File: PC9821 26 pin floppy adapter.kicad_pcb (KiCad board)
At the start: 2 copper layers, 52.7 x 28.6 mm, 3 parts

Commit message: Final version that I just sent off to Osh
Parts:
- added G***: LOGO, Logos:skull-silk, B.Cu at (149.9, 92.7)
- PC98-F1: footprint Connector_IDC:IDC-Header_2x13_P2.54mm_Vertical -> Connector_IDC:IDC-Header_2x13_P2.54mm_Horizontal
- moved POWER1 27.5 mm to (151.8, 69.8), turned to 0 degrees
- moved PC98-F1 24.7 mm to (160.7, 78.7), turned to 0 degrees
- moved GOTEK1 13.5 mm to (139.7, 114.3), turned to 180 degrees
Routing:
- net /WRITE_PROTECT: track 13.9 -> 70.7 mm
- net /TRACK_00: track 13.9 -> 67.9 mm
- net /INDEX_OUT: track 13.9 -> 63.3 mm
- net /SIDE: track 13.9 -> 57.5 mm
- net /WRITE_ENABLE: track 13.9 -> 54.5 mm
- net /READ_DATA: track 13.9 -> 53.4 mm
- net /WRITE_DATA: track 13.9 -> 49.1 mm
- net /DRV_SELECT_0: track 13.9 -> 44.5 mm
- net /STEP_PULSE: track 13.9 -> 39.4 mm, vias 0 -> 2
- net /MOTOR_ON: track 13.9 -> 33.5 mm, vias 0 -> 2
- net /HEAD_LOAD: track 54.9 -> 36.1 mm
- net /DIRECTION: track 14.0 -> 28.1 mm
- net /DRV_SELECT_1: track 17.7 -> 29.8 mm
- net /360_300_DRV_0: track 102.5 -> 114.6 mm, vias 0 -> 4
- net /READY_OUT: track 47.4 -> 36.3 mm, vias 0 -> 1
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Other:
- board size 52.7 x 28.6 mm -> 33.7 x 49.5 mm
- board text added: "25"
- board text added: "34"
- board text added: "nec pc-9821 34-pin floppy adapter v1.0"
- board text added: "www.leadedsolder.com"
- board text removed: "2"
- board text removed: "26"
- board text removed: "33"
- board text removed: "key this end"
- board text removed: "leadedsolder.com"
- board text removed: "pc9821 floppy adapter v1.0"

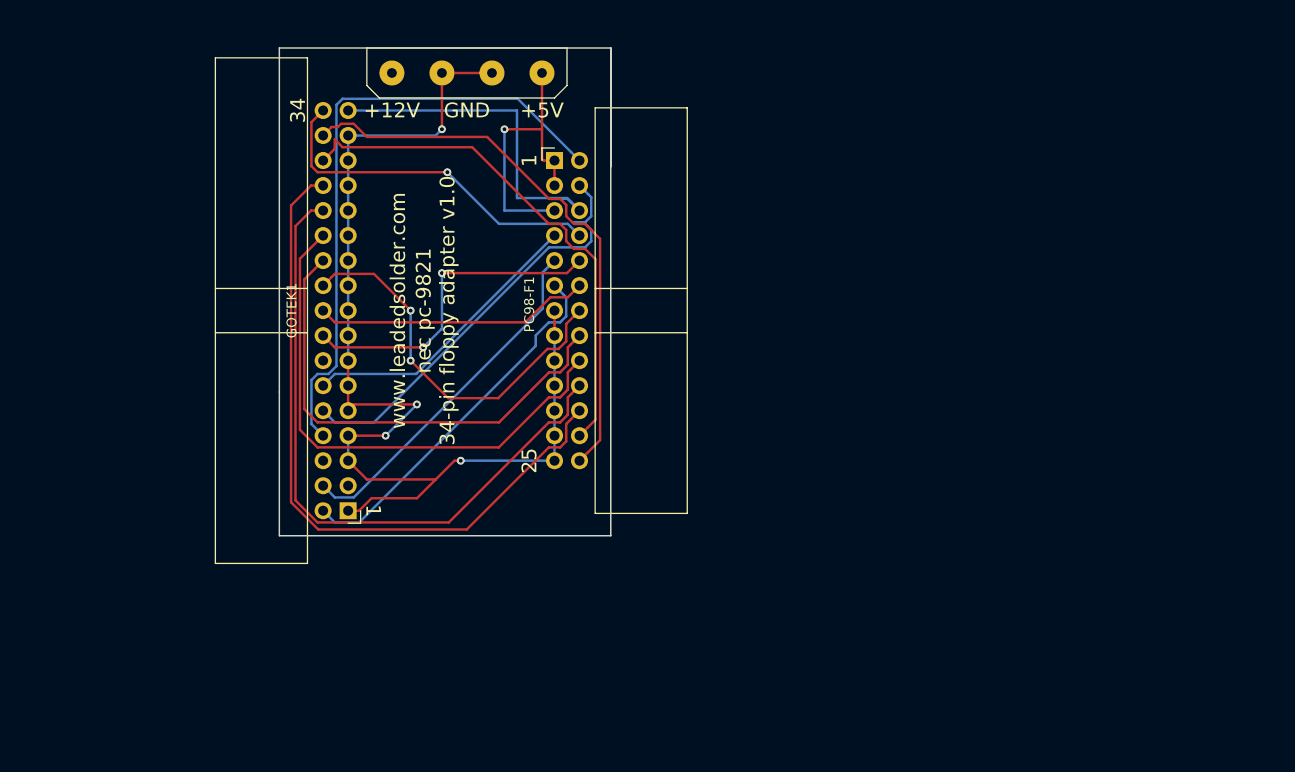
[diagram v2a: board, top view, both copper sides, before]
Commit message: v1.1, a huge ridiculous board that doesn't have a molex power connector on it anymore
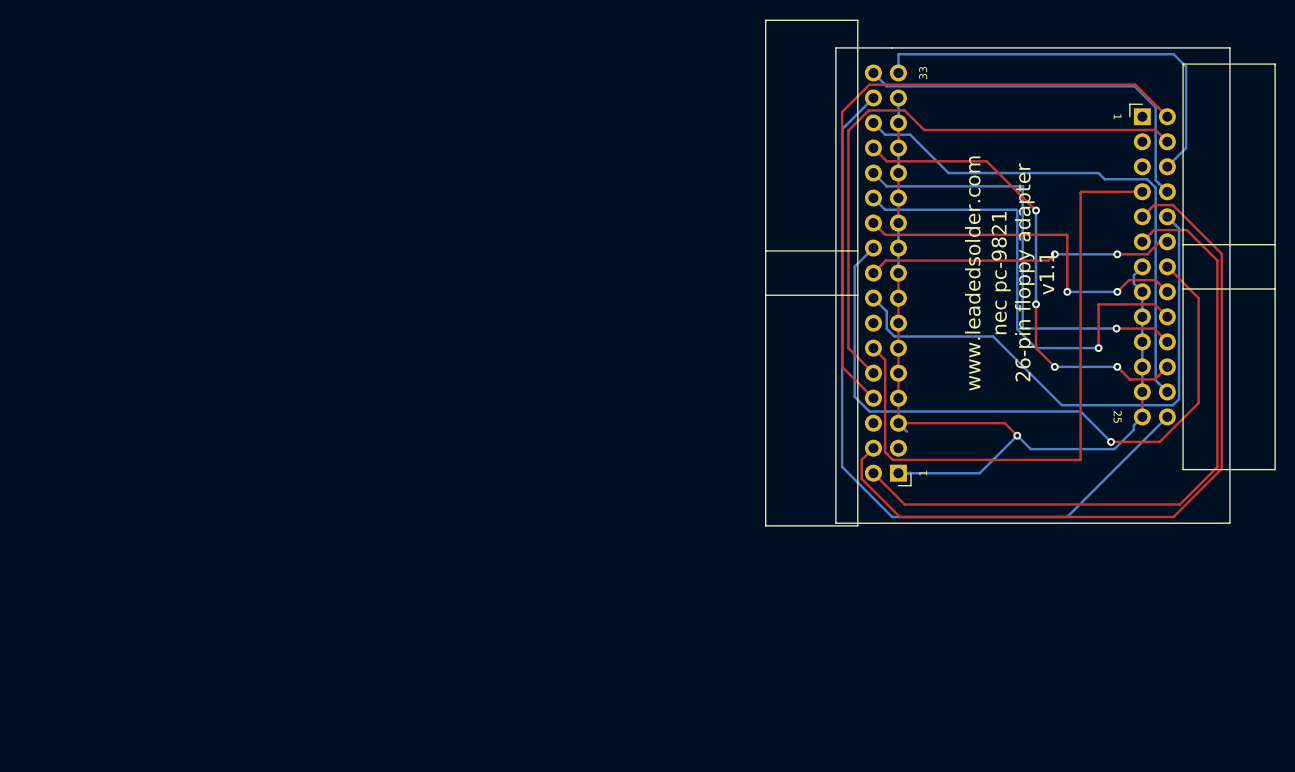
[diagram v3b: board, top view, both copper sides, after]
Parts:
- removed POWER1: 4 pin male molex power, XESS connector lib:xess-MOLEX-8981-04P
- moved PC98-F1 59.9 mm to (220.3, 74.3)
- moved G*** 56.6 mm to (206.4, 90.2)
- moved GOTEK1 56.0 mm to (195.6, 110.5)
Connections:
- PC98-F1 pad 1: /+5V -> /+5V_1
- PC98-F1 pad 3: /+5V -> /+5V_2
- PC98-F1 pad 5: /+5V -> /+5V_3
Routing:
- net /HEAD_LOAD: track 36.1 -> 76.2 mm
- net /DRV_SELECT_1: track 29.8 -> 64.7 mm
- net /DENSITY: track 38.1 -> 68.2 mm
- net /STEP_PULSE: track 39.4 -> 69.5 mm, vias 2 -> 1
- net /+5V: track 29.8 -> 0.00 mm, vias 1 -> 0
- net /WRITE_PROTECT: track 70.7 -> 48.3 mm, vias 0 -> 4
- net /MOTOR_ON: track 33.5 -> 55.8 mm, vias 2 -> 0
- net /TRACK_00: track 67.9 -> 45.6 mm, vias 0 -> 1
- net /360_300_DRV_0: track 114.6 -> 92.5 mm, vias 4 -> 1
- net /SIDE: track 57.5 -> 78.1 mm
- net /DRV_SELECT_0: track 44.5 -> 60.2 mm
- net /WRITE_DATA: track 49.1 -> 37.1 mm, vias 0 -> 2
- net /WRITE_ENABLE: track 54.5 -> 48.2 mm, vias 0 -> 1
- net /DISK_CHANGE: track 36.5 -> 42.6 mm
- net /DIRECTION: track 28.1 -> 31.2 mm, vias 0 -> 2
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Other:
- board size 33.7 x 49.5 mm -> 40 x 48.3 mm
- board text added: "33"
- board text added: "360/300"
- board text added: "nec pc-9821 26-pin floppy adapter v1.1"
- board text removed: "+12V"
- board text removed: "+5V"
- board text removed: "34"
- board text removed: "GND"
- board text removed: "nec pc-9821 34-pin floppy adapter v1.0"

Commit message: Minaturized version, now only 7.95 instead of 15.05
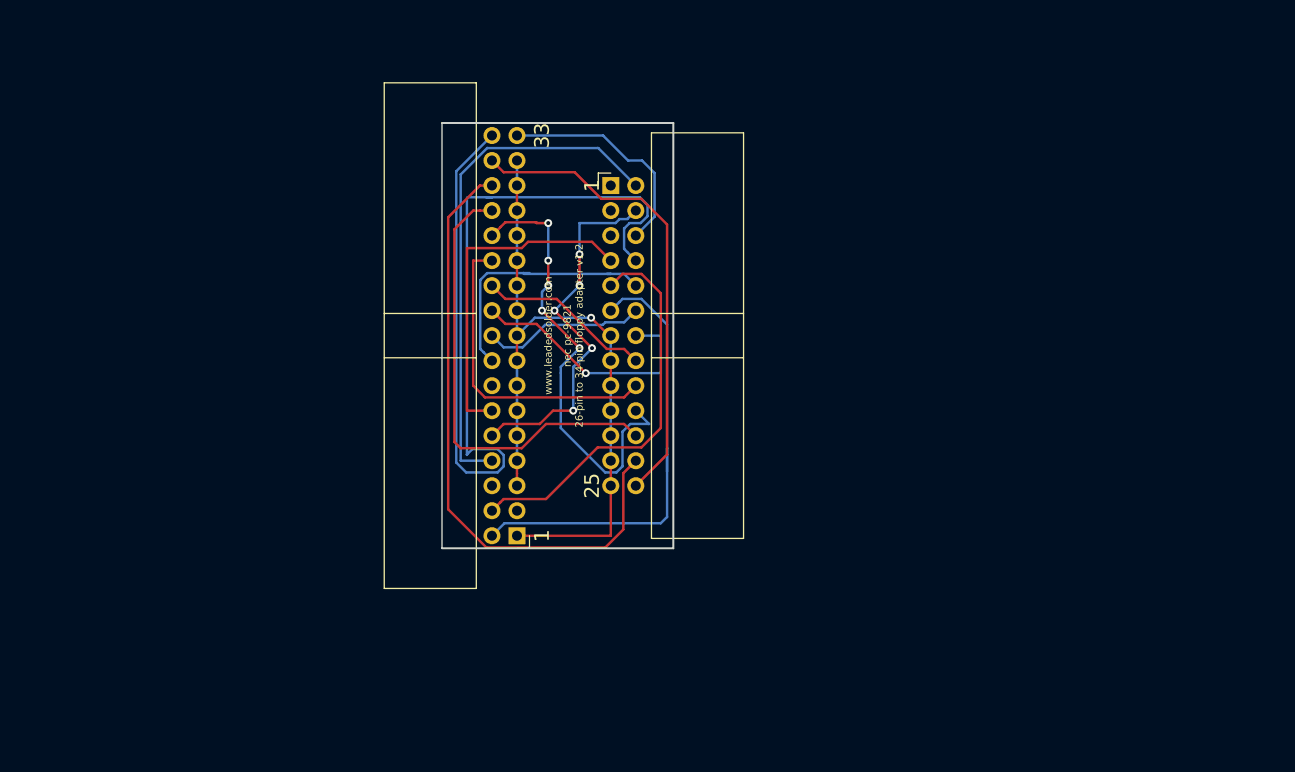
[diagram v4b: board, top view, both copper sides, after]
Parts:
- removed G***: LOGO, Logos:skull-silk
- moved PC98-F1 54.4 mm to (166.4, 81.3)
- moved GOTEK1 39.3 mm to (156.8, 116.8)
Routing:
- net /READY_OUT: track 39.2 -> 98.9 mm
- net /STEP_PULSE: track 69.5 -> 26.1 mm
- net /HEAD_LOAD: track 76.2 -> 40.7 mm
- net /DRV_SELECT_1: track 64.7 -> 34.7 mm
- net /SIDE: track 78.1 -> 48.3 mm
- net /MOTOR_ON: track 55.8 -> 26.3 mm
- net /DRV_SELECT_0: track 60.2 -> 38.0 mm, vias 0 -> 5
- net /DENSITY: track 68.2 -> 47.8 mm
- net /DISK_CHANGE: track 42.6 -> 22.7 mm
- net /WRITE_DATA: track 37.1 -> 17.8 mm, vias 2 -> 0
- net /360_300_DRV_0: track 92.5 -> 73.9 mm
- net /WRITE_ENABLE: track 48.2 -> 32.1 mm, vias 1 -> 0
- net /DIRECTION: track 31.2 -> 16.6 mm, vias 2 -> 0
- net /INDEX_OUT: track 65.9 -> 52.7 mm
- net /READ_DATA: track 52.6 -> 63.8 mm
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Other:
- board size 40 x 48.3 mm -> 23.5 x 43.2 mm
- board text added: "idc 34-pin female"
- board text added: "nec 26-pin male"
- board text added: "nec pc-9821 26-pin to 34-pin floppy adapter v1.2"
- board text removed: "360/300"
- board text removed: "nec pc-9821 26-pin floppy adapter v1.1"

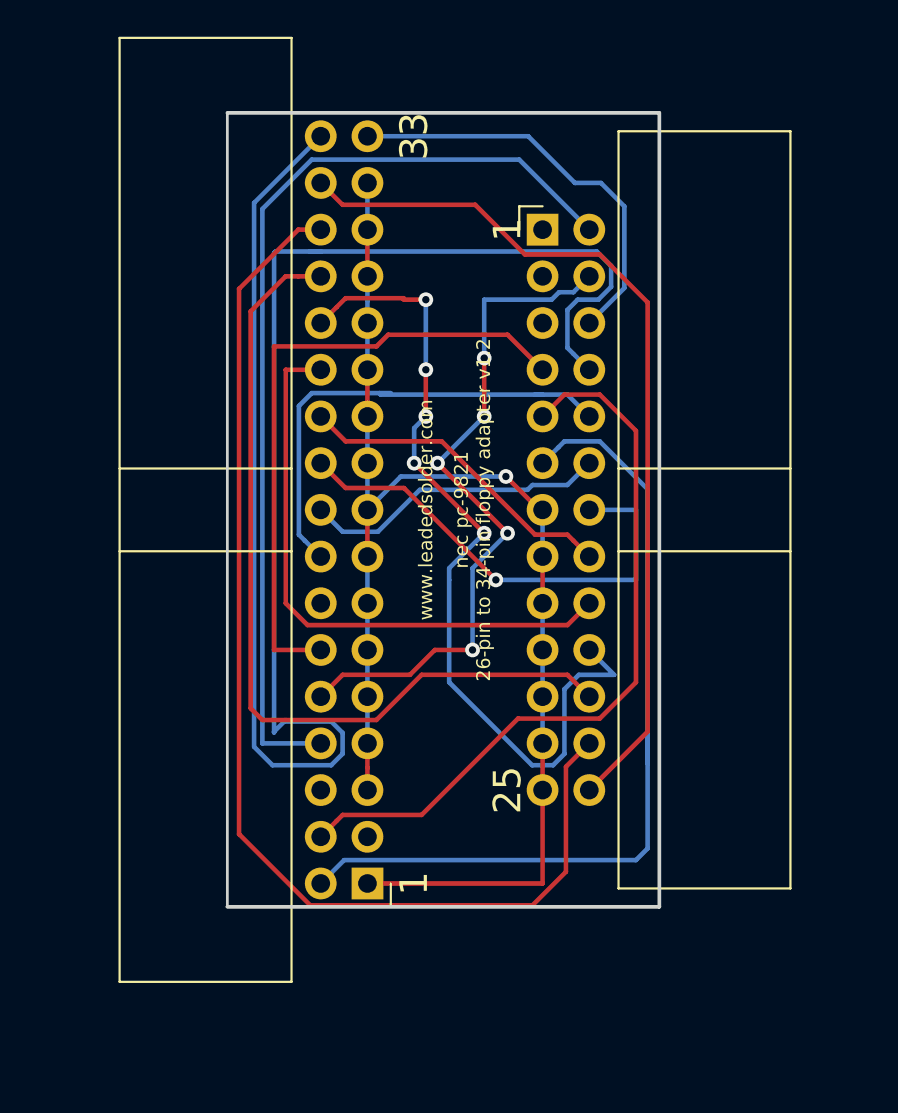
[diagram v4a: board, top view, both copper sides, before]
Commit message: A revision with a Molex 8981 power connector to provide power OUT to the 34-pin floppy drive
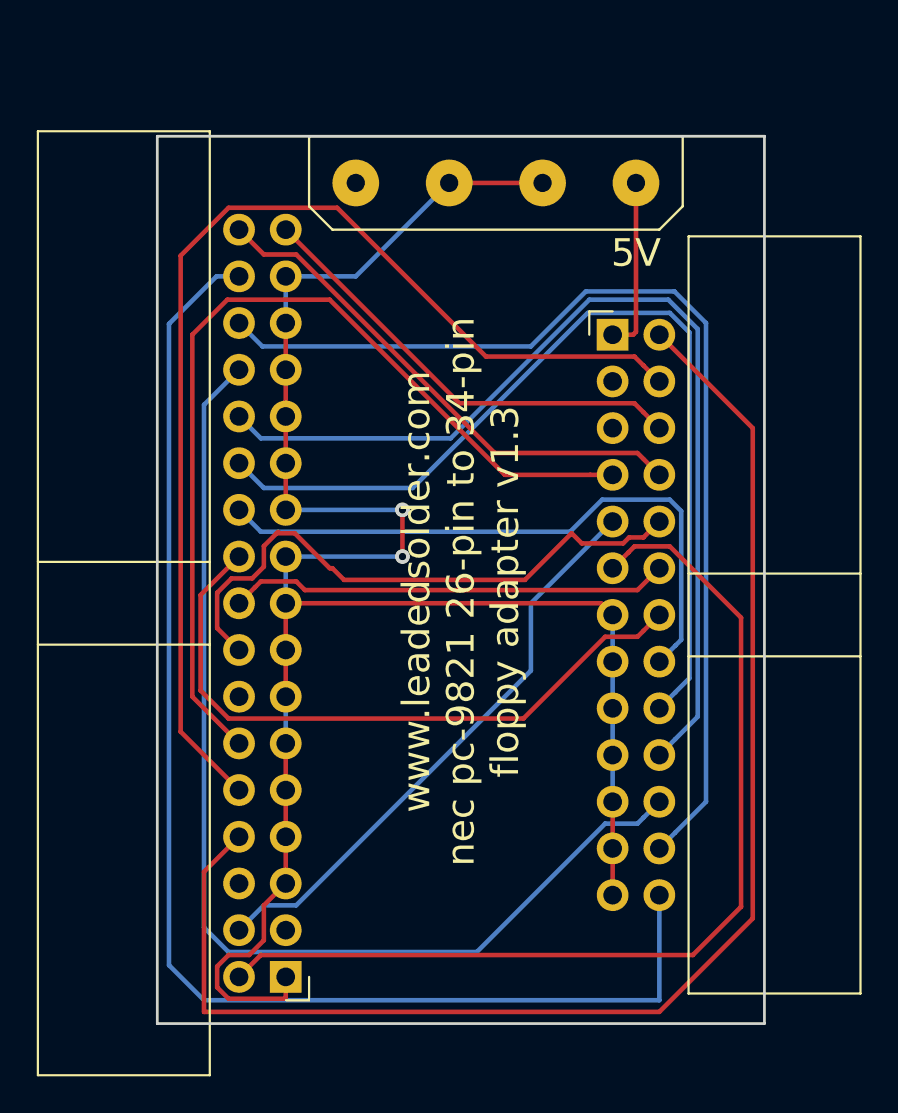
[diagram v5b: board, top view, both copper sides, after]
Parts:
- added PWR1: Molex 8981 Power Out, XESS connector lib:xess-MOLEX-8981-04P, F.Cu at (163.8, 78.7)
- moved PC98-F1 6.87 mm to (170.2, 87.0)
- moved GOTEK1 6.75 mm to (152.4, 121.9)
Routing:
- net /READY_OUT: track 98.9 -> 28.4 mm
- net /360_300_DRV_0: track 73.9 -> 108.1 mm, vias 1 -> 2
- net /SIDE: track 48.3 -> 72.9 mm
- net /INDEX_OUT: track 52.7 -> 76.1 mm
- net /DRV_SELECT_0: track 38.0 -> 61.4 mm, vias 5 -> 0
- net /WRITE_ENABLE: track 32.1 -> 50.6 mm
- net /WRITE_DATA: track 17.8 -> 34.2 mm
- net /DRV_SELECT_1: track 34.7 -> 50.9 mm
- net /WRITE_PROTECT: track 46.4 -> 59.8 mm
- net /STEP_PULSE: track 26.1 -> 36.1 mm, vias 1 -> 0
- net /+5V_1: track 0.00 -> 9.43 mm
- net /HEAD_LOAD: track 40.7 -> 31.7 mm
- net /DIRECTION: track 16.6 -> 24.0 mm
- net /TRACK_00: track 46.7 -> 53.3 mm, vias 5 -> 0
- net /READ_DATA: track 63.8 -> 57.5 mm
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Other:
- board size 23.5 x 43.2 mm -> 33 x 48.3 mm
- board text added: "5V"
- board text added: "POWER OUT"
- board text added: "www.leadedsolder.com nec pc-9821 26-pin to 34-pin floppy adapter v1.3"
- board text removed: "idc 34-pin female"
- board text removed: "nec 26-pin male"
- board text removed: "nec pc-9821 26-pin to 34-pin floppy adapter v1.2"
- board text removed: "www.leadedsolder.com"

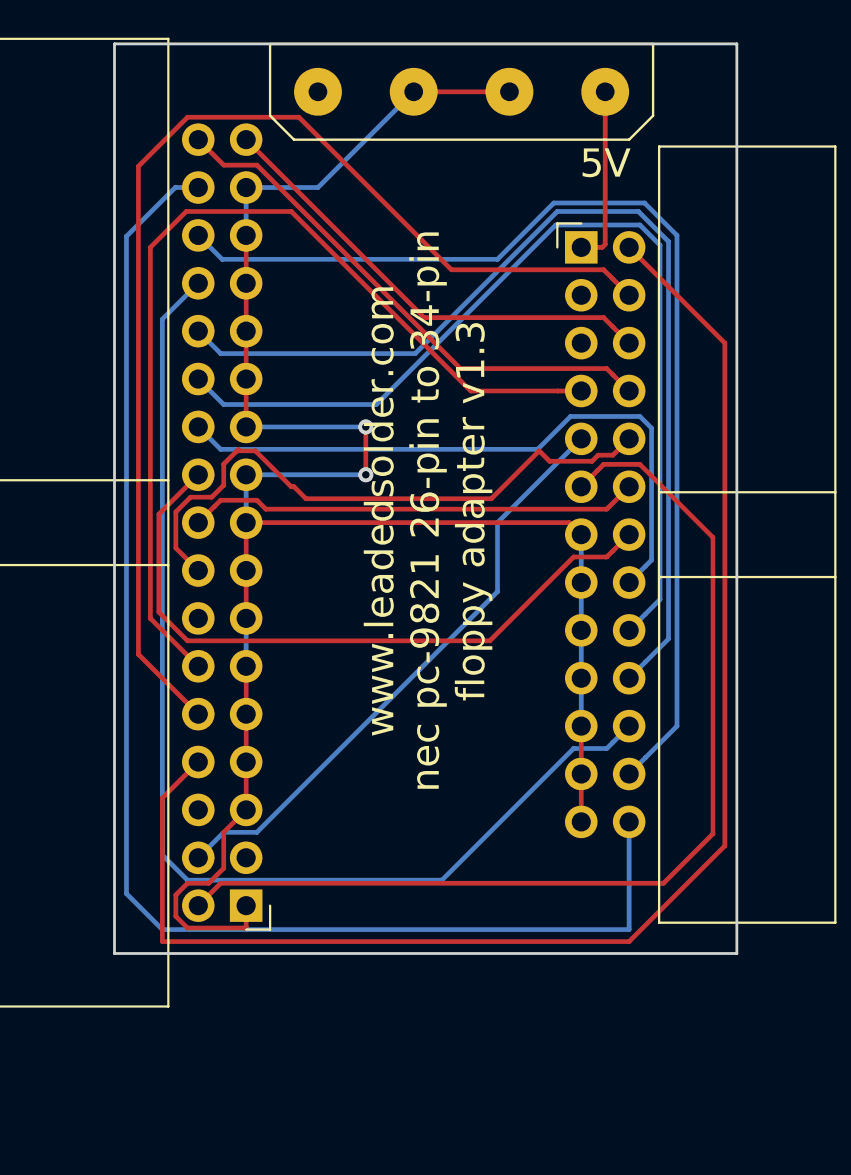
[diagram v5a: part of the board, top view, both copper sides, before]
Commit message: Revision 1.4 - has bigger holes for the Molex connector, and the Molex connector is on the other side
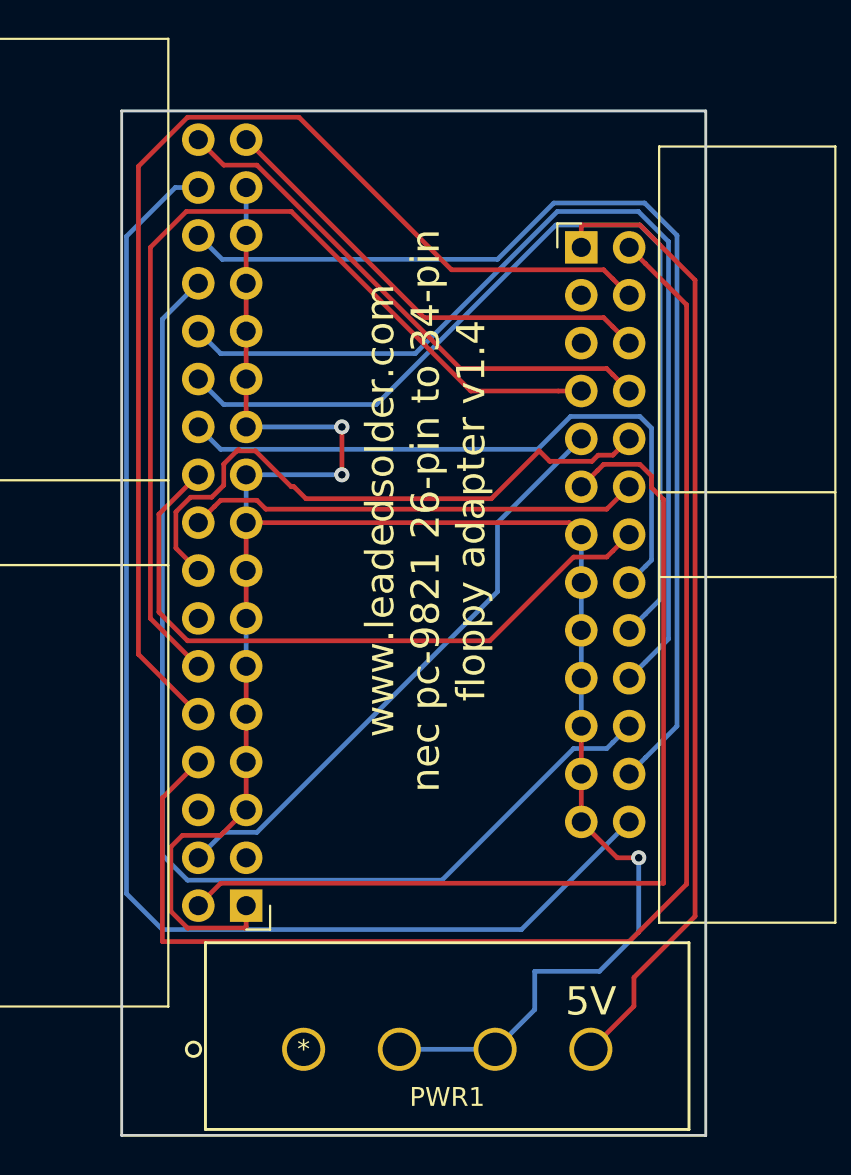
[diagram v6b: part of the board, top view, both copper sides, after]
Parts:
- PWR1: footprint XESS connector lib:xess-MOLEX-8981-04P -> 7709971:770997-1
- moved PWR1 51.5 mm to (155.4, 129.5), turned to 180 degrees
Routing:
- net /+5V_1: track 9.43 -> 51.5 mm
- net /360_300_DRV_0: track 108.1 -> 114.4 mm, vias 2 -> 3
- net /SIDE: track 72.9 -> 69.6 mm
- net /DENSITY: track 53.7 -> 51.5 mm
- net /INDEX_OUT: track 76.1 -> 74.4 mm
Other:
- board size 33 x 48.3 mm -> 31 x 54.4 mm
- board text added: "www.leadedsolder.com nec pc-9821 26-pin to 34-pin floppy adapter v1.4"
- board text removed: "POWER OUT"
- board text removed: "www.leadedsolder.com nec pc-9821 26-pin to 34-pin floppy adapter v1.3"
